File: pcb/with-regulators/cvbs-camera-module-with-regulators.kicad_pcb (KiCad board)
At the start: 4 copper layers, 35 x 33 mm, 17 parts, among them J1 X.FL-PR-SMT1-2(80), J2 5052740612, J3 X.FL-R-SMT-1(02), J5 Conn_01x03, J6 X.FL-R-SMT-1(02), U1 cvbs-camera, U2 TPS8269xxxSIPR, U3 NCP163AFCT250T2G

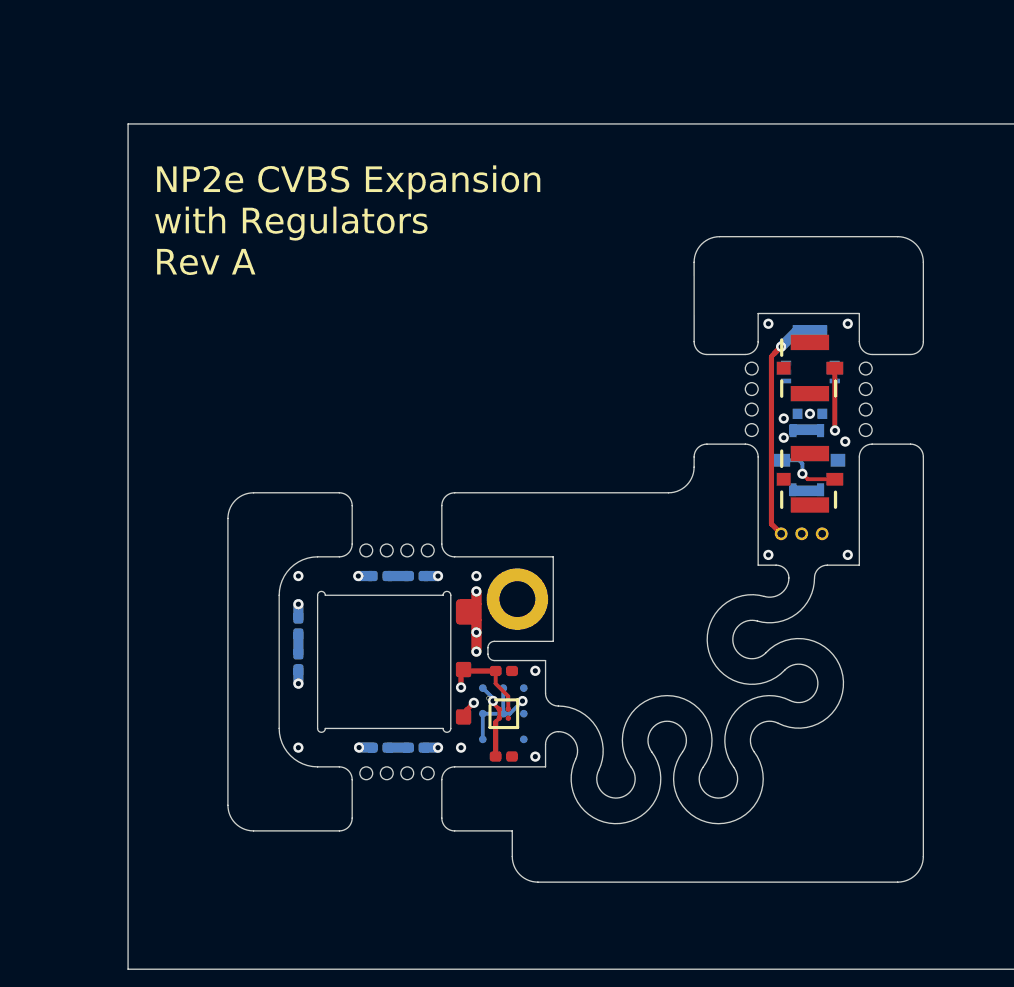
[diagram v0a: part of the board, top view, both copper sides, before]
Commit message: Address feedback
- Fill out title blocks
- LEDs 0201 -> 0402 & assign PN
- Power LEDs with 2.85V regulator
- Remove noise on fab layers
- Thicken flex cable
- Add .sldprt & .dxf files for flex pattern
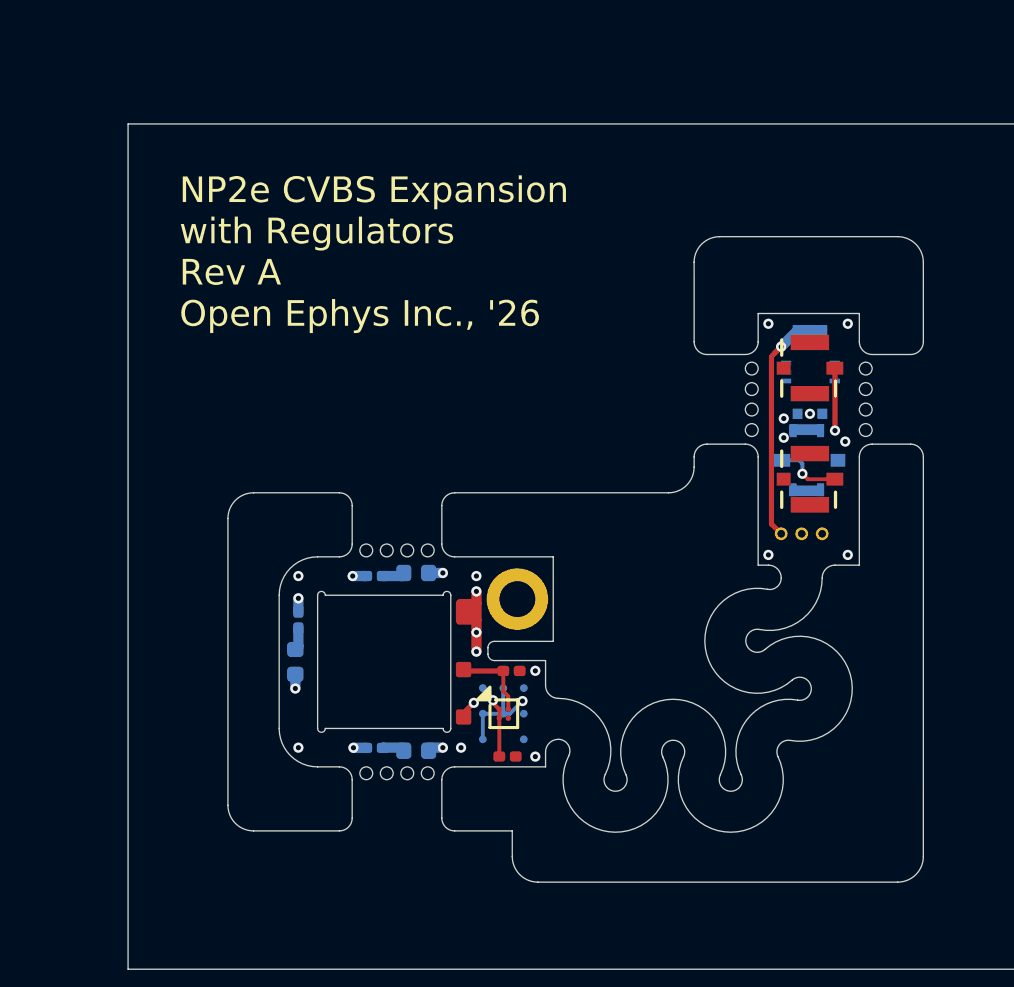
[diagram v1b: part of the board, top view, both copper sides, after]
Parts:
- D1, D2, D3: value LED -> IN-S42CTQIR; footprint LED_SMD:LED_0201_0603Metric -> LED_SMD:LED_0402_1005Metric
- U2: value TPS8269xxxSIPR -> TPS82693SIPR
- moved C2 0.30 mm to (103.0, 69.4)
- moved R1 0.23 mm to (94.7, 67.4)
- moved R3 0.22 mm to (97.6, 72.4)
- moved R2 0.22 mm to (97.6, 65.7)
- moved C1 0.14 mm to (102.8, 72.7)
- moved D1 0.12 mm to (94.5, 69.0)
- moved D2 0.12 mm to (99.2, 65.5)
- moved D3 0.12 mm to (99.2, 72.5)
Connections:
- C1 pad 1: Net-(U2-VOUT) -> +2V8
- R1 pad 1: +2V5 -> +2V8
- R2 pad 1: +2V5 -> +2V8
- R3 pad 1: +2V5 -> +2V8
- U2 pad A1: Net-(U2-VOUT) -> +2V8
- U3 pad A1: Net-(U2-VOUT) -> +2V8
- U3 pad B1: Net-(U2-VOUT) -> +2V8
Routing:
- net +2V8: track 0.00 -> 4.58 mm, vias 0 -> 4
- net Net-(U2-VOUT): track 3.00 -> 0.00 mm, vias 1 -> 0
- net +2V5: track 5.30 -> 3.29 mm, vias 4 -> 0
- added copper zone on In1.Cu, net +2V8
- removed copper zone on In1.Cu, net +2V5
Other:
- outline, holes or cut-outs redrawn
- board text added: "NP2e CVBS Expansion with Regulators Rev A Open Ephys Inc., '26"
- board text removed: "NP2e CVBS Expansion with Regulators Rev A"
